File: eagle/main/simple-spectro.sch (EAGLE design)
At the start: 55 parts, among them CON1 BAT, CON2 SPI, CON3 SPI, CON4 VIBR, IC1 32U4, IC2 MCP73831T, IC4 DMP1045U or DMG2302, IC5 LM1117S-3.3, Q6 BSP75, U1 NCT75DMR2G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

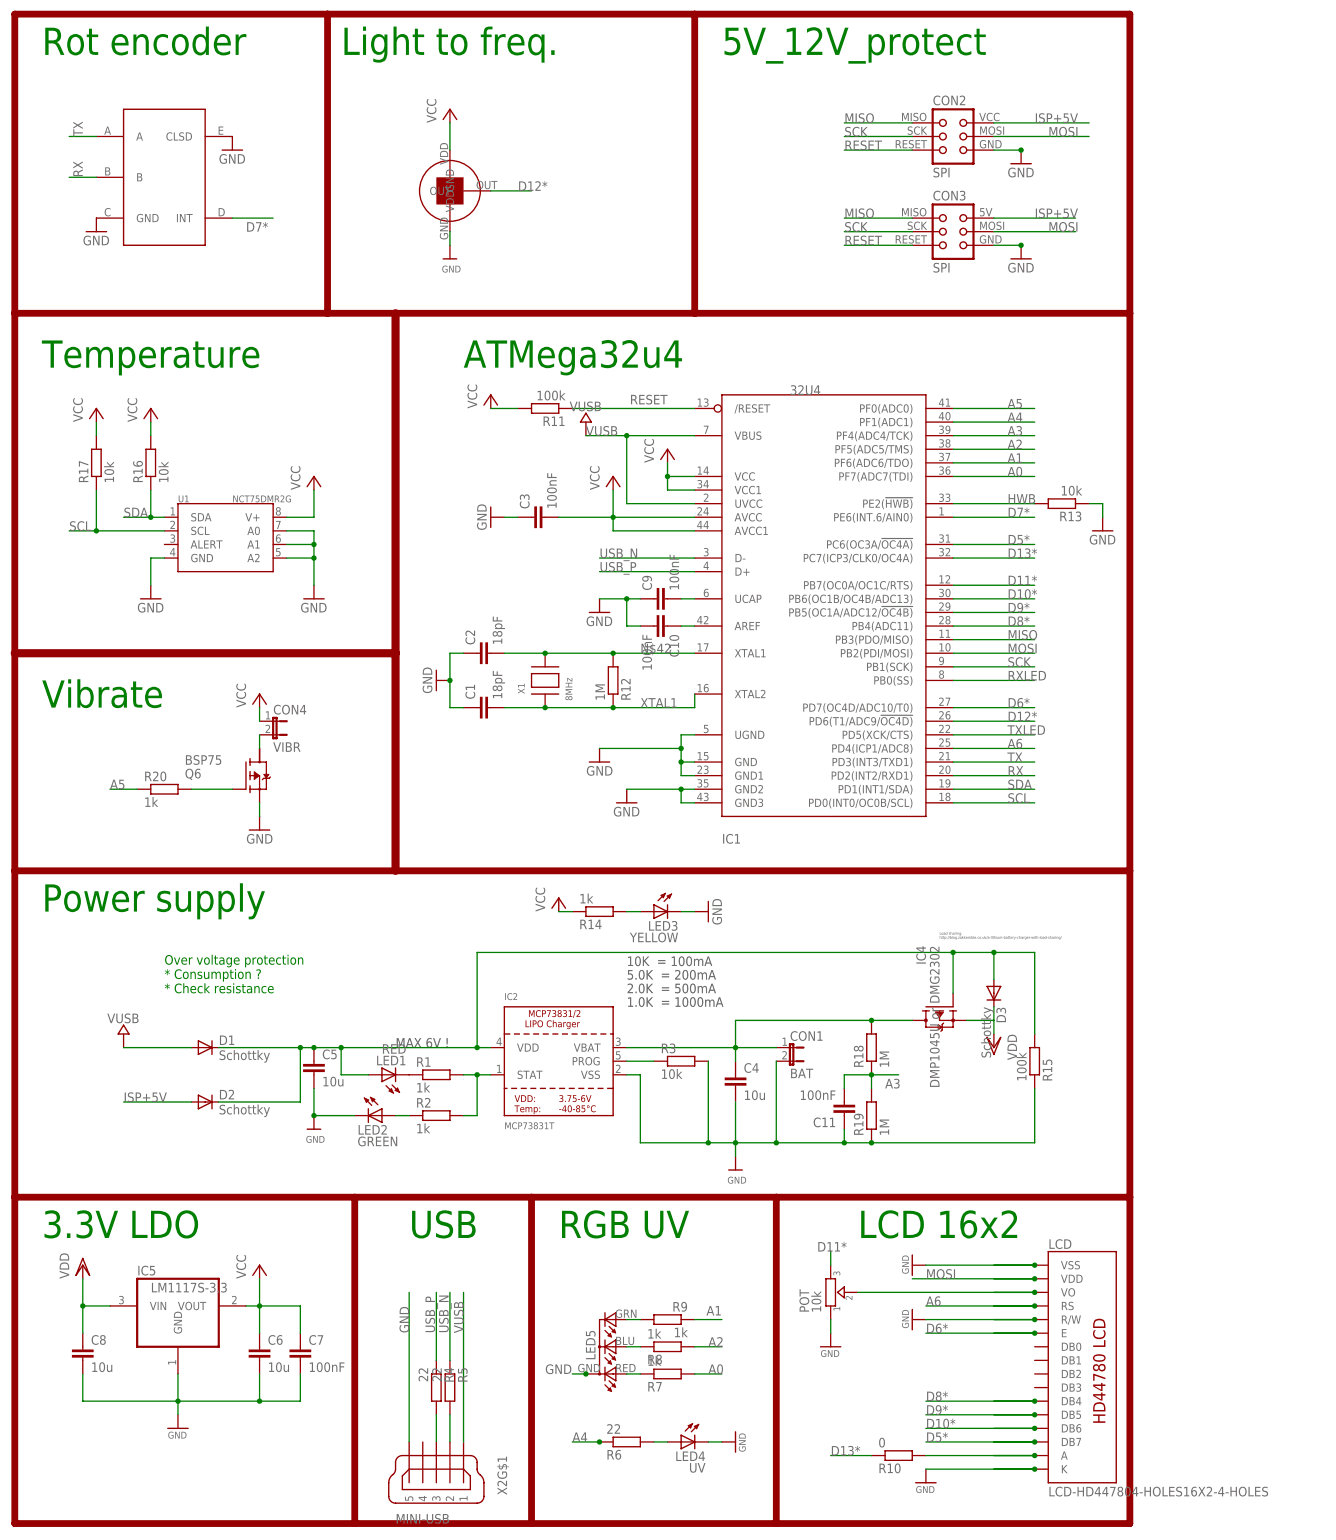
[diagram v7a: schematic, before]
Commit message: atmega32u4 power the TSL and temperature
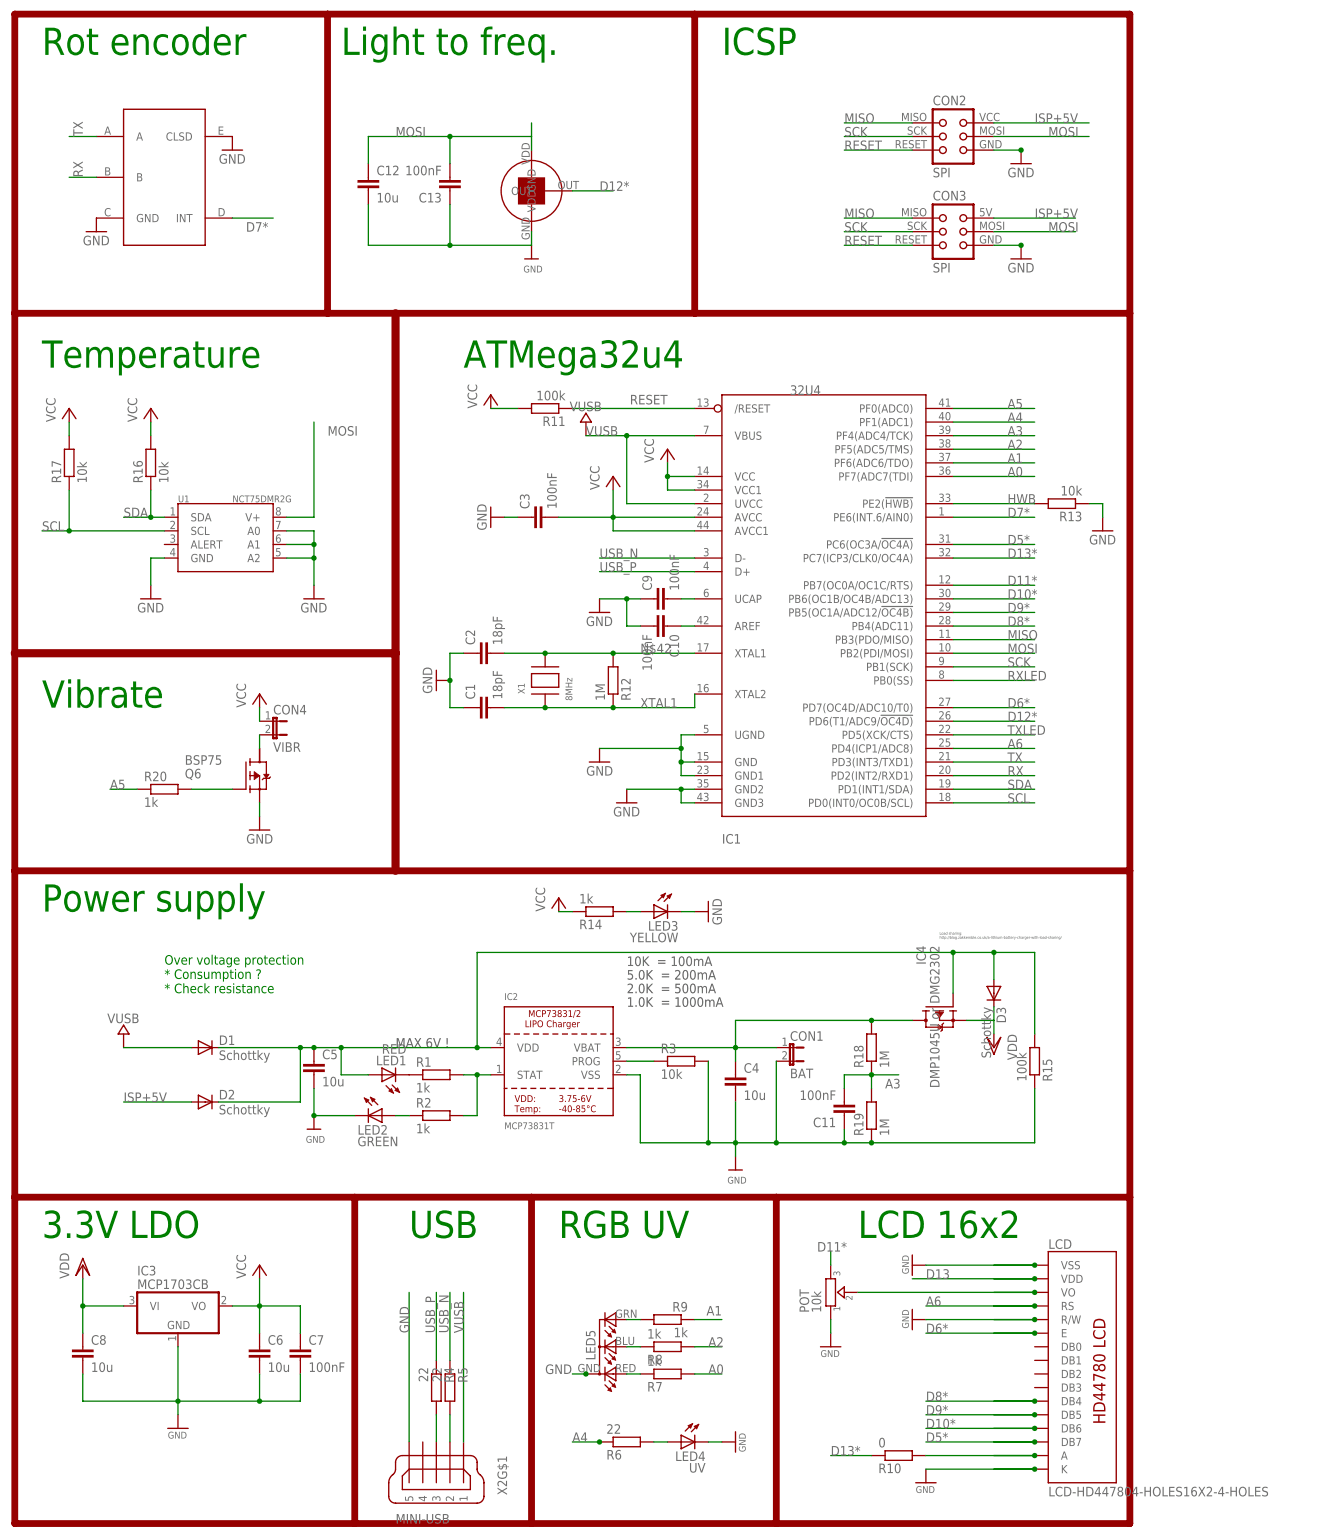
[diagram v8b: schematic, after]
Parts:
- removed IC5: LM1117S-3.3, burr-brown:REG1117
- added C12: 10u, rcl:C-EUC0805K
- added C13: 100nF, rcl:C-EUC0805K
- added IC3: MCP1703CB, linear:MCP1703CB
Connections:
- new net D13: LCD.VDD
- net GND: now also C12.2, C13.1, IC3.GND; no longer IC5.GND
- net MOSI: now also C12.1, C13.2, U$7.VDD, U1.V+; no longer LCD.VDD
- net VCC: now also IC3.VO; no longer IC5.VOUT, U$7.VDD, U1.V+
- net VDD: now also IC3.VI; no longer IC5.VIN
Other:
- note added: "ICSP"
- note removed: "5V_12V_protect"
- moved on the sheet: R17
